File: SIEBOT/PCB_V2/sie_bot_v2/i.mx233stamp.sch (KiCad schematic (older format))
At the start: 0 parts

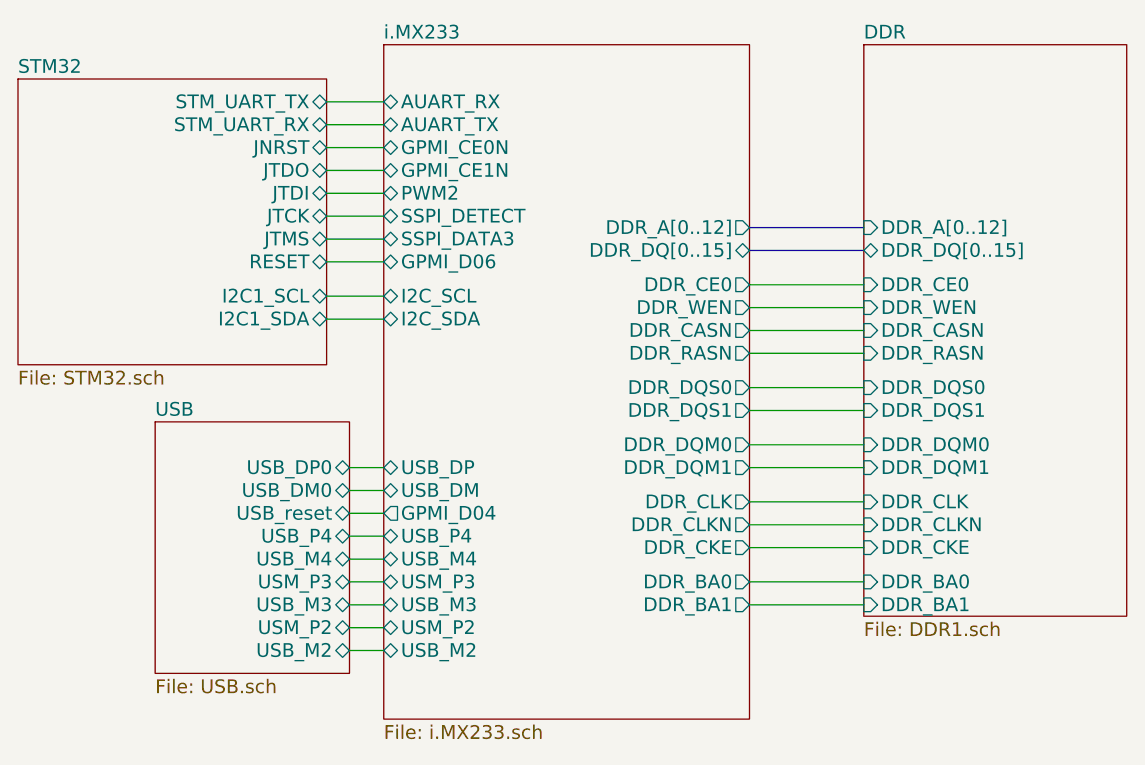
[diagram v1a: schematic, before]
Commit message: Adición del Jack de alimentación, se agregó una señal BOOT_MODE para cambiar la señal BOOT0 del stm32
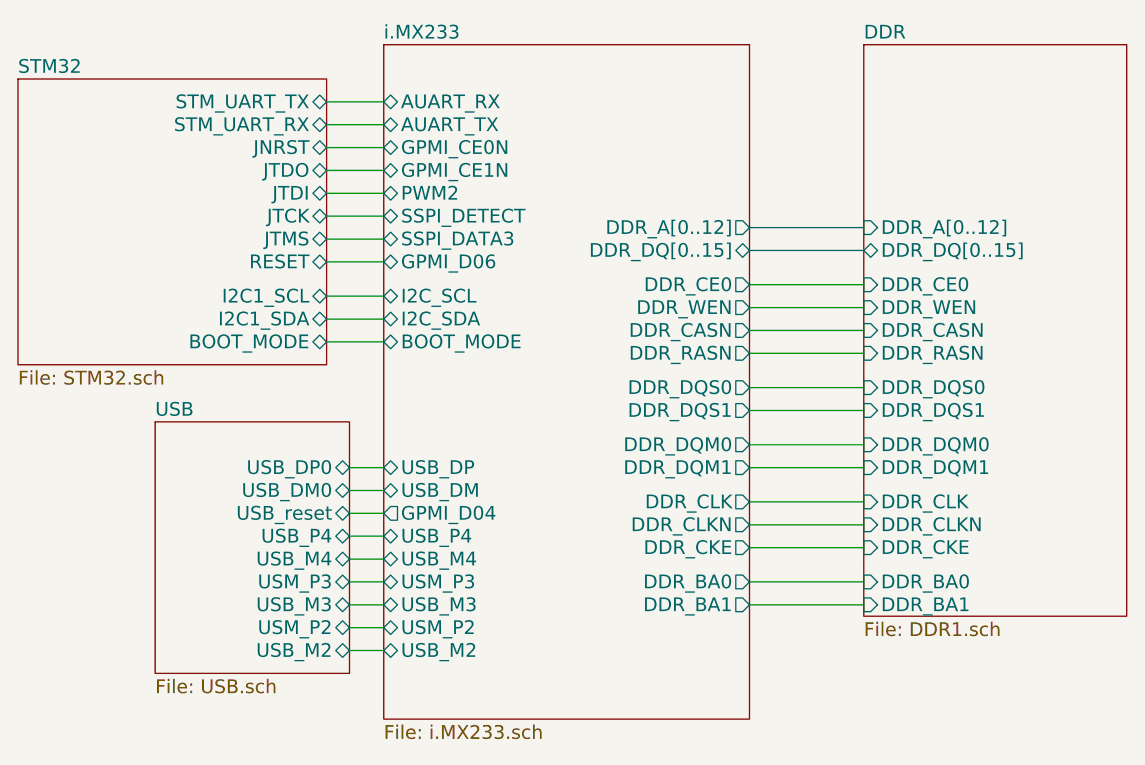
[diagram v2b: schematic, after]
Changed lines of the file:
@@
-EESchema Schematic File Version 2  date Fri 30 Mar 2012 08:38:46 AM COT
+EESchema Schematic File Version 2  date Thu 19 Jul 2012 05:56:15 PM COT
 LIBS:con-jack
 LIBS:adm3101e
@@
 Sheet 1 5
 Title ""
-Date "30 mar 2012"
+Date "19 jul 2012"
 Rev ""
 Comp ""
@@
 $EndDescr
 Wire Wire Line
-	3000 3650 3150 3650
-Wire Wire Line
-	2900 1850 3150 1850
-Wire Wire Line
-	2900 2700 3150 2700
-Wire Wire Line
-	3000 4150 3150 4150
-Wire Wire Line
-	2900 2450 3150 2450
-Wire Wire Line
-	2900 2350 3150 2350
-Wire Wire Line
-	2900 2150 3150 2150
-Wire Wire Line
-	3000 3950 3150 3950
-Wire Wire Line
-	3000 3750 3150 3750
-Wire Wire Line
-	3150 3450 3000 3450
+	2900 2900 3150 2900
+Wire Wire Line
+	2900 1950 3150 1950
+Wire Wire Line
+	3150 2800 2900 2800
+Wire Wire Line
+	3000 4250 3150 4250
+Wire Wire Line
+	2900 2550 3150 2550
+Wire Wire Line
+	2900 2250 3150 2250
+Wire Wire Line
+	2900 2050 3150 2050
+Wire Wire Line
+	3000 4050 3150 4050
+Wire Wire Line
+	3000 3850 3150 3850
+Wire Wire Line
+	3000 3550 3150 3550
+Wire Bus Line
+	5250 2400 4750 2400
+Wire Wire Line
+	4750 3450 5250 3450
+Wire Wire Line
+	5250 3200 4750 3200
+Wire Wire Line
+	4750 2950 5250 2950
+Wire Wire Line
+	4750 4050 5250 4050
+Wire Wire Line
+	4750 3800 5250 3800
+Wire Wire Line
+	4750 3600 5250 3600
+Wire Wire Line
+	4750 2850 5250 2850
+Wire Wire Line
+	4750 2750 5250 2750
+Wire Wire Line
+	4750 2650 5250 2650
+Wire Wire Line
+	4750 3700 5250 3700
+Wire Wire Line
+	4750 3950 5250 3950
+Wire Wire Line
+	4750 3100 5250 3100
+Wire Wire Line
+	5250 3350 4750 3350
 Wire Bus Line
 	4750 2500 5250 2500
 Wire Wire Line
-	5250 3350 4750 3350
-Wire Wire Line
-	4750 3100 5250 3100
-Wire Wire Line
-	4750 3950 5250 3950
-Wire Wire Line
-	4750 3700 5250 3700
-Wire Wire Line
-	4750 2650 5250 2650
-Wire Wire Line
-	4750 2750 5250 2750
-Wire Wire Line
-	4750 2850 5250 2850
-Wire Wire Line
-	4750 3600 5250 3600
-Wire Wire Line
-	4750 3800 5250 3800
-Wire Wire Line
-	4750 4050 5250 4050
-Wire Wire Line
-	4750 2950 5250 2950
-Wire Wire Line
-	5250 3200 4750 3200
-Wire Wire Line
-	4750 3450 5250 3450
-Wire Bus Line
-	5250 2400 4750 2400
-Wire Wire Line
-	3000 3550 3150 3550
-Wire Wire Line
-	3000 3850 3150 3850
-Wire Wire Line
-	3000 4050 3150 4050
-Wire Wire Line
-	2900 2050 3150 2050
-Wire Wire Line
-	2900 2250 3150 2250
-Wire Wire Line
-	2900 2550 3150 2550
-Wire Wire Line
-	3000 4250 3150 4250
-Wire Wire Line
-	3150 2800 2900 2800
-Wire Wire Line
-	2900 1950 3150 1950
+	3150 3450 3000 3450
+Wire Wire Line
+	3000 3750 3150 3750
+Wire Wire Line
+	3000 3950 3150 3950
+Wire Wire Line
+	2900 2150 3150 2150
+Wire Wire Line
+	2900 2350 3150 2350
+Wire Wire Line
+	2900 2450 3150 2450
+Wire Wire Line
+	3000 4150 3150 4150
+Wire Wire Line
+	2900 2700 3150 2700
+Wire Wire Line
+	2900 1850 3150 1850
+Wire Wire Line
+	3000 3650 3150 3650
 $Sheet
 S 3150 1600 1600 2950
@@
 F34 "PWM2" B L 3150 2250 60
 F35 "GPMI_D04" O L 3150 3650 60
+F36 "BOOT_MODE" B L 3150 2900 60
 $EndSheet
 $Sheet
@@
 F10 "STM_UART_TX" B R 2900 1850 60
 F11 "STM_UART_RX" B R 2900 1950 60
+F12 "BOOT_MODE" B R 2900 2900 60
 $EndSheet
 $Sheet

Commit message: USB device connector has been added
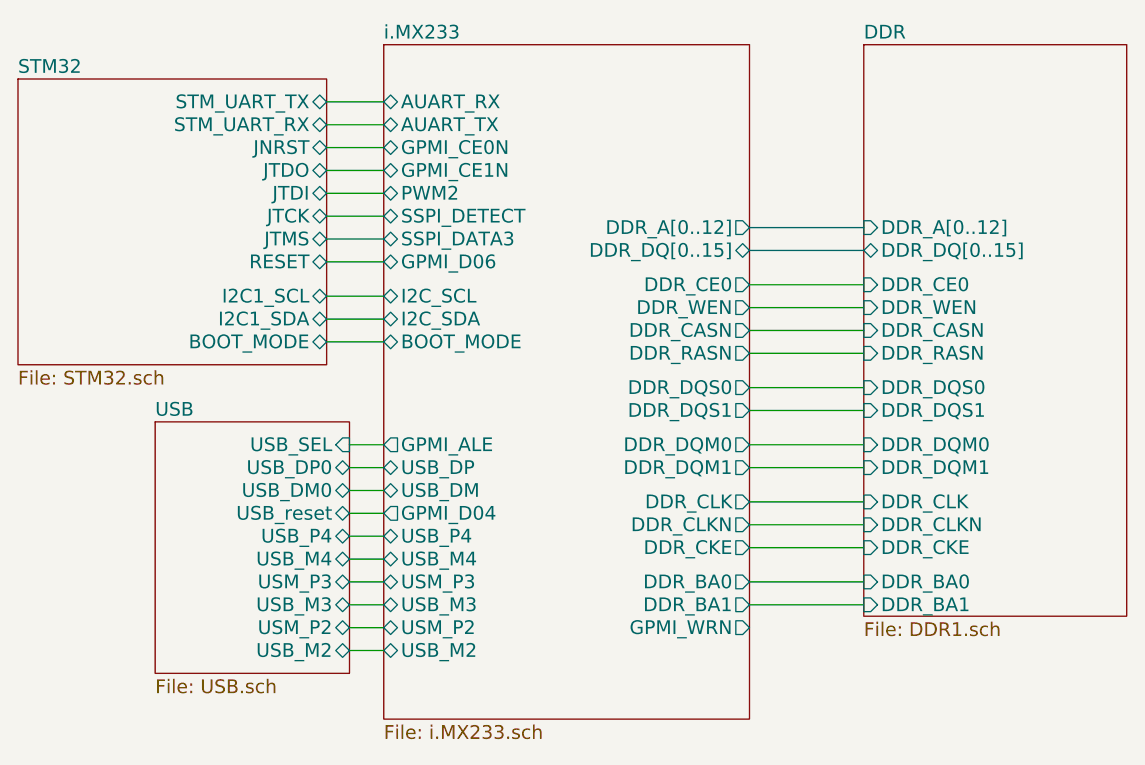
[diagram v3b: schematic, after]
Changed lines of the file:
@@
-EESchema Schematic File Version 2  date Thu 19 Jul 2012 05:56:15 PM COT
+EESchema Schematic File Version 2  date Wed 15 Aug 2012 11:19:40 AM COT
 LIBS:con-jack
 LIBS:adm3101e
@@
 LIBS:lt1117cst
 LIBS:zxmhc3f381n8
+LIBS:fsusb43
+LIBS:usb-mini
 LIBS:i.mx233stamp-cache
 EELAYER 25  0
 EELAYER END
-$Descr A4 11700 8267
+$Descr A4 11693 8268
 encoding utf-8
 Sheet 1 5
 Title ""
-Date "19 jul 2012"
+Date "15 aug 2012"
 Rev ""
 Comp ""
@@
 Comment4 ""
 $EndDescr
-Wire Wire Line
-	2900 2900 3150 2900
-Wire Wire Line
-	2900 1950 3150 1950
-Wire Wire Line
-	3150 2800 2900 2800
-Wire Wire Line
-	3000 4250 3150 4250
-Wire Wire Line
-	2900 2550 3150 2550
-Wire Wire Line
-	2900 2250 3150 2250
-Wire Wire Line
-	2900 2050 3150 2050
-Wire Wire Line
-	3000 4050 3150 4050
-Wire Wire Line
-	3000 3850 3150 3850
-Wire Wire Line
-	3000 3550 3150 3550
-Wire Bus Line
-	5250 2400 4750 2400
-Wire Wire Line
-	4750 3450 5250 3450
-Wire Wire Line
-	5250 3200 4750 3200
-Wire Wire Line
-	4750 2950 5250 2950
-Wire Wire Line
-	4750 4050 5250 4050
-Wire Wire Line
-	4750 3800 5250 3800
-Wire Wire Line
-	4750 3600 5250 3600
-Wire Wire Line
-	4750 2850 5250 2850
-Wire Wire Line
-	4750 2750 5250 2750
-Wire Wire Line
-	4750 2650 5250 2650
-Wire Wire Line
-	4750 3700 5250 3700
-Wire Wire Line
-	4750 3950 5250 3950
-Wire Wire Line
-	4750 3100 5250 3100
-Wire Wire Line
-	5250 3350 4750 3350
-Wire Bus Line
-	4750 2500 5250 2500
-Wire Wire Line
-	3150 3450 3000 3450
-Wire Wire Line
-	3000 3750 3150 3750
-Wire Wire Line
-	3000 3950 3150 3950
-Wire Wire Line
-	2900 2150 3150 2150
-Wire Wire Line
-	2900 2350 3150 2350
-Wire Wire Line
-	2900 2450 3150 2450
-Wire Wire Line
-	3000 4150 3150 4150
-Wire Wire Line
-	2900 2700 3150 2700
-Wire Wire Line
-	2900 1850 3150 1850
-Wire Wire Line
-	3000 3650 3150 3650
 $Sheet
 S 3150 1600 1600 2950
@@
 F35 "GPMI_D04" O L 3150 3650 60
 F36 "BOOT_MODE" B L 3150 2900 60
+F37 "GPMI_WRN" O R 4750 4150 60
+F38 "GPMI_ALE" O L 3150 3350 60
 $EndSheet
 $Sheet
@@
 F9 "USM_P2" B R 3000 4150 60
 F10 "USB_reset" B R 3000 3650 60
-$EndSheet
+F11 "USB_SEL" I R 3000 3350 60
+$EndSheet
+Wire Wire Line
+	2900 2900 3150 2900
+Wire Wire Line
+	2900 1950 3150 1950
+Wire Wire Line
+	3150 2800 2900 2800
+Wire Wire Line
+	3000 4250 3150 4250
+Wire Wire Line
+	2900 2550 3150 2550
+Wire Wire Line
+	2900 2250 3150 2250
+Wire Wire Line
+	2900 2050 3150 2050
+Wire Wire Line
+	3000 4050 3150 4050
+Wire Wire Line
+	3000 3850 3150 3850
+Wire Wire Line
+	3000 3550 3150 3550
+Wire Bus Line
+	5250 2400 4750 2400
+Wire Wire Line
+	4750 3450 5250 3450
+Wire Wire Line
+	5250 3200 4750 3200
+Wire Wire Line
+	4750 2950 5250 2950
+Wire Wire Line
+	4750 4050 5250 4050
+Wire Wire Line
+	4750 3800 5250 3800
+Wire Wire Line
+	4750 3600 5250 3600
+Wire Wire Line
+	4750 2850 5250 2850
+Wire Wire Line
+	4750 2750 5250 2750
+Wire Wire Line
+	4750 2650 5250 2650
+Wire Wire Line
+	4750 3700 5250 3700
+Wire Wire Line
+	4750 3950 5250 3950
+Wire Wire Line
+	4750 3100 5250 3100
+Wire Wire Line
+	5250 3350 4750 3350
+Wire Bus Line
+	4750 2500 5250 2500
+Wire Wire Line
+	3150 3450 3000 3450
+Wire Wire Line
+	3000 3750 3150 3750
+Wire Wire Line
+	3000 3950 3150 3950
+Wire Wire Line
+	2900 2150 3150 2150
+Wire Wire Line
+	2900 2350 3150 2350
+Wire Wire Line
+	2900 2450 3150 2450
+Wire Wire Line
+	3000 4150 3150 4150
+Wire Wire Line
+	2900 2700 3150 2700
+Wire Wire Line
+	2900 1850 3150 1850
+Wire Wire Line
+	3000 3650 3150 3650
+Wire Wire Line
+	3150 3350 3000 3350
 $EndSCHEMATC
